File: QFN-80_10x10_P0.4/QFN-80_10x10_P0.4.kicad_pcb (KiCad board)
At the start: 2 copper layers, 25.4 x 106.7 mm, 10 parts, among them J101 Conn_01x40, J102 Conn_01x40, J103 Conn_01x40, J104 Conn_01x40, J105 Conn_01x02, J106 Conn_01x02, J107 Conn_01x02, J108 Conn_01x02, U101 QFN-80

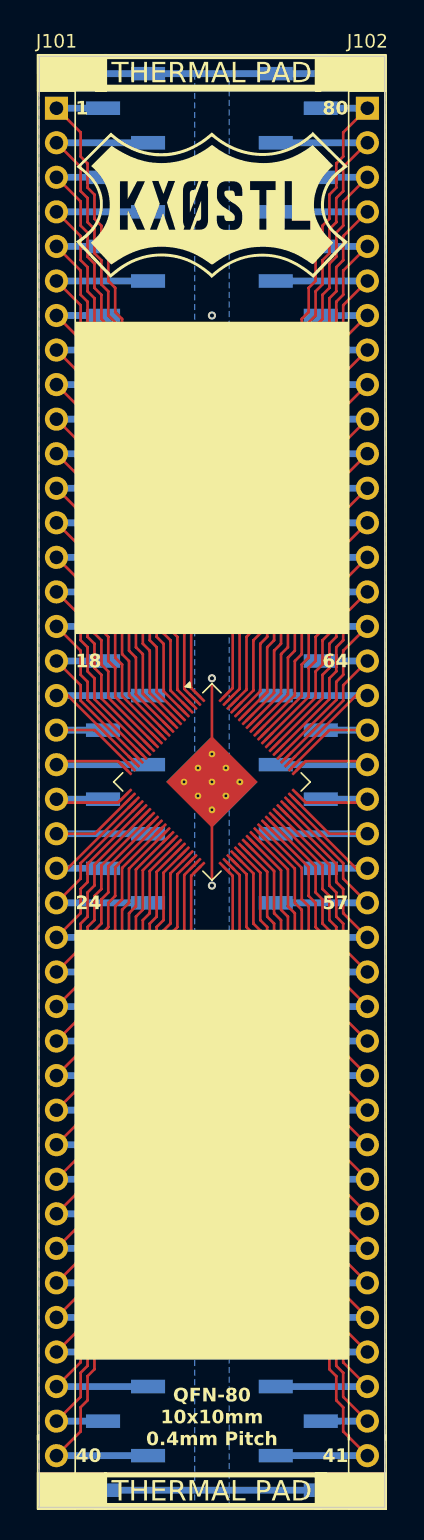
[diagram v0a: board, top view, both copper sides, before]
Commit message: Created SMDIP-16, QFP-48, QFP-32, QFN-80, QFN-68, QFN-64, QFN-60, QFN-56, QFN-48, QFN-36, QFN-28, QFN-20, QFP-32, QFP-48
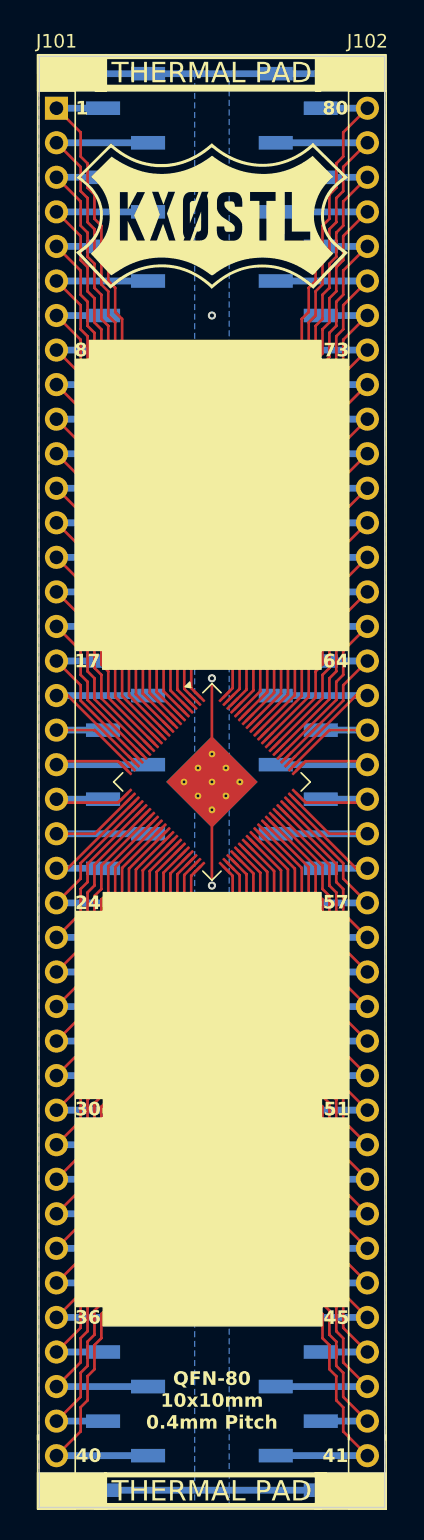
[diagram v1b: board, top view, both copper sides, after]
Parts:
- moved G*** 0.80 mm to (138.4, 86.6)
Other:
- board text added: "17"
- board text added: "30"
- board text added: "36"
- board text added: "45"
- board text added: "51"
- board text added: "73"
- board text added: "8"
- board text removed: "18"
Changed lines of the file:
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@@
 	(footprint "libraries:LogoSmall"
 		(layer "F.Cu")
-		(at 138.43 85.852)
+		(at 138.43 86.649039)
 		(property "Reference" "G***"
 			(at 0 0 0)
@@
 			(thermal_bridge_angle 90)
 		)
-		(pad "2" thru_hole rect
+		(pad "2" thru_hole circle
 			(at 0 2.54)
 			(size 1.7 1.7)
@@
 			(pinfunction "Pin_2")
 			(pintype "passive")
-			(thermal_bridge_angle 45)
 		)
 		(pad "3" thru_hole circle
@@
 	)
 	(gr_rect
-		(start 128.397 139.192)
-		(end 148.463 170.688)
+		(start 130.44 136.404363)
+		(end 146.456 137.814363)
+		(stroke
+			(width 0.1)
+			(type solid)
+		)
+		(fill yes)
+		(layer "F.SilkS")
+	)
+	(gr_rect
+		(start 128.397 152.977)
+		(end 148.463 166.838)
 		(stroke
 			(width 0.1)
@@
 	)
 	(gr_rect
+		(start 129.419999 95.811085)
+		(end 146.445999 97.441085)
+		(stroke
+			(width 0.1)
+			(type solid)
+		)
+		(fill yes)
+		(layer "F.SilkS")
+	)
+	(gr_rect
+		(start 130.397 118.355)
+		(end 146.453 119.985)
+		(stroke
+			(width 0.1)
+			(type solid)
+		)
+		(fill yes)
+		(layer "F.SilkS")
+	)
+	(gr_rect
 		(start 125.603 179.06975)
 		(end 130.6745 181.737)
@@
 	)
 	(gr_rect
+		(start 128.437 137.7895)
+		(end 148.483 151.5405)
+		(stroke
+			(width 0.1)
+			(type solid)
+		)
+		(fill yes)
+		(layer "F.SilkS")
+	)
+	(gr_rect
+		(start 130.447 145.779)
+		(end 146.483 159.64)
+		(stroke
+			(width 0.1)
+			(type solid)
+		)
+		(fill yes)
+		(layer "F.SilkS")
+	)
+	(gr_rect
 		(start 146.0415 179.06975)
 		(end 151.24 181.737)
@@
 	)
 	(gr_rect
-		(start 128.397 94.488)
-		(end 148.463 117.348)
+		(start 128.397 97.198)
+		(end 148.463 118.608)
 		(stroke
 			(width 0.1)
@@
 		(layer "F.SilkS")
 	)
+	(gr_rect
+		(start 130.437 166.707)
+		(end 146.523 168.26)
+		(stroke
+			(width 0.1)
+			(type solid)
+		)
+		(fill yes)
+		(layer "F.SilkS")
+	)
 	(gr_line
 		(start 125.73 181.61)
@@
 		)
 	)
+	(gr_text "45"
+		(at 148.54 167.65 0)
+		(layer "F.SilkS" knockout)
+		(effects
+			(font
+				(size 1 1)
+				(thickness 0.2)
+				(bold yes)
+			)
+			(justify right)
+		)
+	)
+	(gr_text "8"
+		(at 128.32 96.52 0)
+		(layer "F.SilkS" knockout)
+		(effects
+			(font
+				(size 1 1)
+				(thickness 0.2)
+				(bold yes)
+			)
+			(justify left)
+		)
+	)
 	(gr_text "24"
-		(at 128.397 137.16 0)
-		(layer "F.SilkS")
+		(at 128.36 137.16 0)
+		(layer "F.SilkS" knockout)
 		(effects
 			(font
@@
 		)
 	)
+	(gr_text "51"
+		(at 148.55 152.32 0)
+		(layer "F.SilkS" knockout)
+		(effects
+			(font
+				(size 1 1)
+				(thickness 0.2)
+				(bold yes)
+			)
+			(justify right)
+		)
+	)
 	(gr_text "QFN-80\n10x10mm\n0.4mm Pitch"
-		(at 138.43 177.152819 0)
+		(at 138.43 175.938819 0)
 		(layer "F.SilkS")
 		(effects
@@
 	)
 	(gr_text "57"
-		(at 148.463 137.16 0)
-		(layer "F.SilkS")
+		(at 148.49 137.114051 0)
+		(layer "F.SilkS" knockout)
 		(effects
 			(font
@@
 		)
 	)
-	(gr_text "18"
-		(at 128.397 119.38 0)
-		(layer "F.SilkS")
+	(gr_text "36"
+		(at 128.36 167.64 0)
+		(layer "F.SilkS" knockout)
+		(effects
+			(font
+				(size 1 1)
+				(thickness 0.2)
+				(bold yes)
+			)
+			(justify left)
+		)
+	)
+	(gr_text "73"
+		(at 148.53 96.52 0)
+		(layer "F.SilkS" knockout)
+		(effects
+			(font
+				(size 1 1)
+				(thickness 0.2)
+				(bold yes)
+			)
+			(justify right)
+		)
+	)
+	(gr_text "30"
+		(at 128.36 152.32 0)
+		(layer "F.SilkS" knockout)
+		(effects
+			(font
+				(size 1 1)
+				(thickness 0.2)
+				(bold yes)
+			)
+			(justify left)
+		)
+	)
+	(gr_text "17"
+		(at 128.32 119.38 0)
+		(layer "F.SilkS" knockout)
 		(effects
 			(font
@@
 	)
 	(gr_text "64"
-		(at 148.463 119.38 0)
-		(layer "F.SilkS")
+		(at 148.49 119.38 0)
+		(layer "F.SilkS" knockout)
 		(effects
 			(font
